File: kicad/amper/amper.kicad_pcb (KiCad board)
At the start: 2 copper layers, 100 x 100 mm, 53 parts, among them J1 Conn_02x05_Odd_Even, J2 Conn_02x05_Odd_Even, J3 Conn_02x05_Odd_Even, J4 USB_C_Receptacle_USB2.0, J5 Conn_01x03, J6 Conn_01x04, J7 Conn_01x05, Q1 FDS9435A, Q2 FDS9435A, SW1 SW_Push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

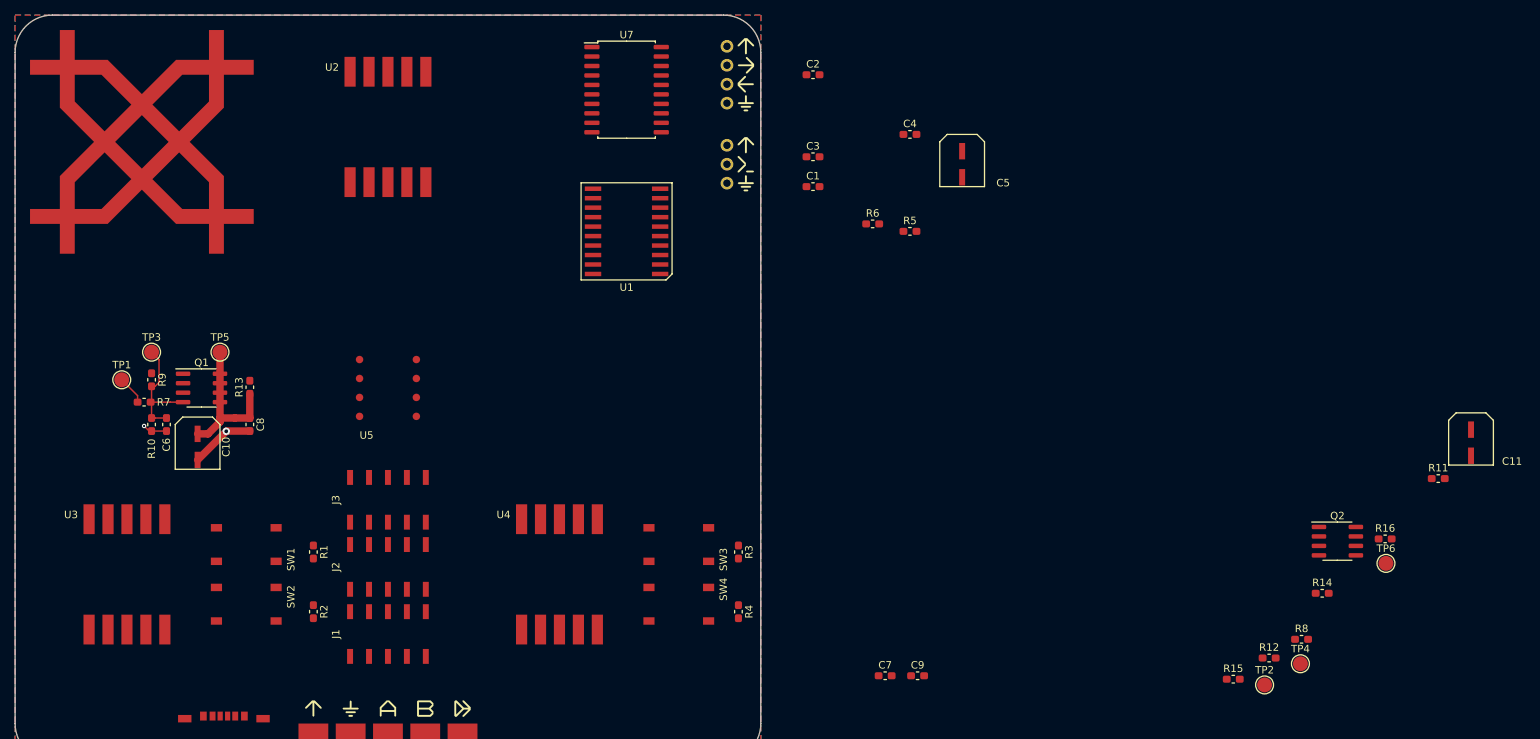
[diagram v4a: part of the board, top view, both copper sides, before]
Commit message: Layed out symetrical 7 seg and driver circuits
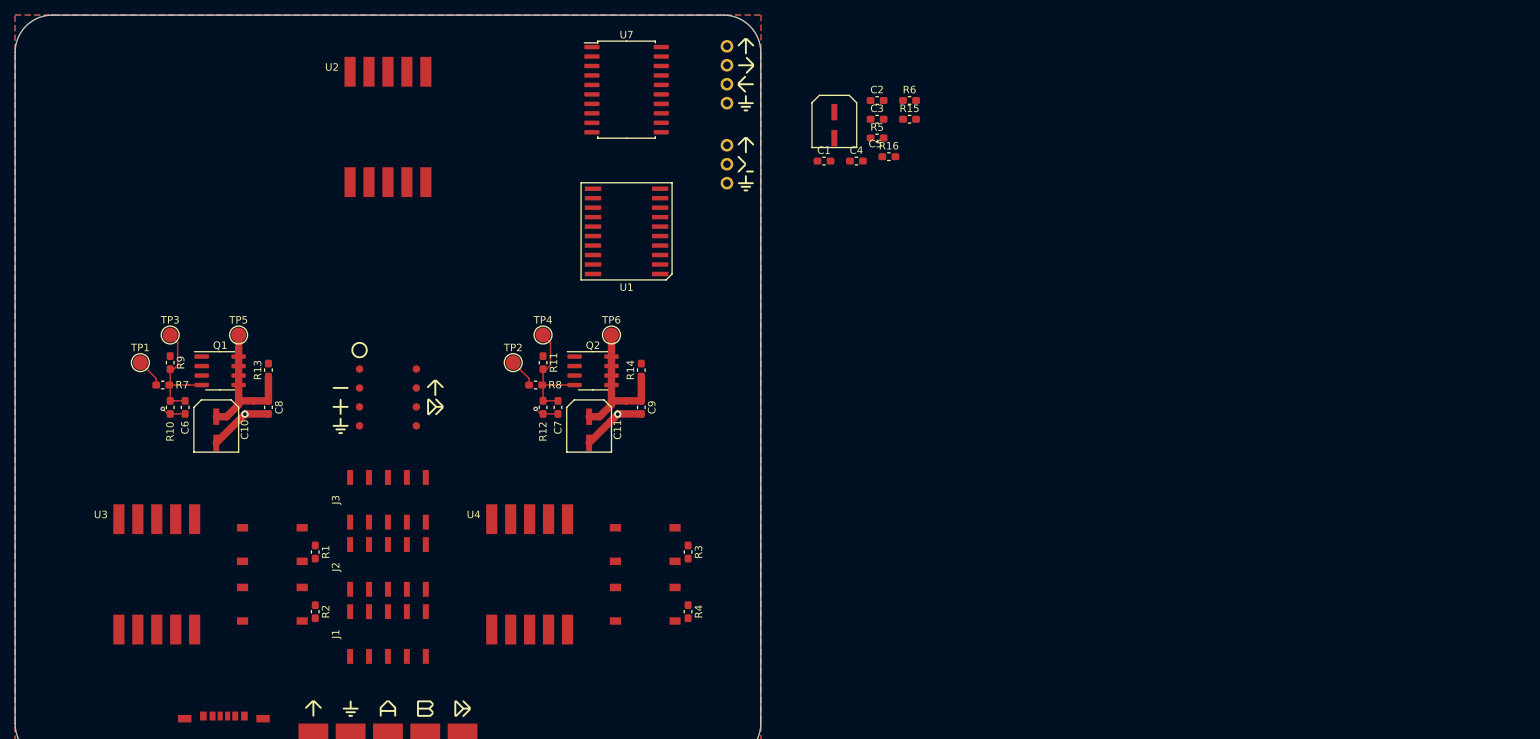
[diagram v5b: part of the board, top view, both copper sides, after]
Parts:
- removed svg2mod: G***, amper:pcb_logo
- U5: footprint amper:114-87-308-41-134161 -> amper:114-87-308-41-134161-generated
- moved R11 121.0 mm to (20.8, -3.40), turned to 270 degrees
- moved C11 118.3 mm to (27.0, 5.61)
- moved TP4 110.7 mm to (20.8, -7.10)
- moved TP2 109.6 mm to (16.8, -3.40)
- moved TP6 108.3 mm to (30.0, -7.10)
- moved R8 108.2 mm to (19.8, -0.40), turned to 180 degrees
- moved R12 103.0 mm to (20.8, 2.60), turned to 270 degrees
- moved Q2 102.4 mm to (27.5, -2.30)
- moved R14 96.1 mm to (34.0, -2.40), turned to 90 degrees
- moved R15 86.7 mm to (69.9, -36.0)
- moved R16 84.0 mm to (67.2, -31.0)
- moved C7 56.7 mm to (22.8, 2.60), turned to 270 degrees
- moved C9 51.7 mm to (34.0, 2.60), turned to 270 degrees
- moved C5 17.9 mm to (59.9, -35.2)
- moved R6 17.3 mm to (69.9, -38.5)
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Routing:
- net /SourceBOut: track 0.00 -> 20.3 mm
- net Net-(C7-Pad1): track 0.00 -> 16.4 mm
- net GND: track 11.9 -> 23.8 mm, vias 2 -> 4
- net /SourceBPwm: track 0.00 -> 3.88 mm

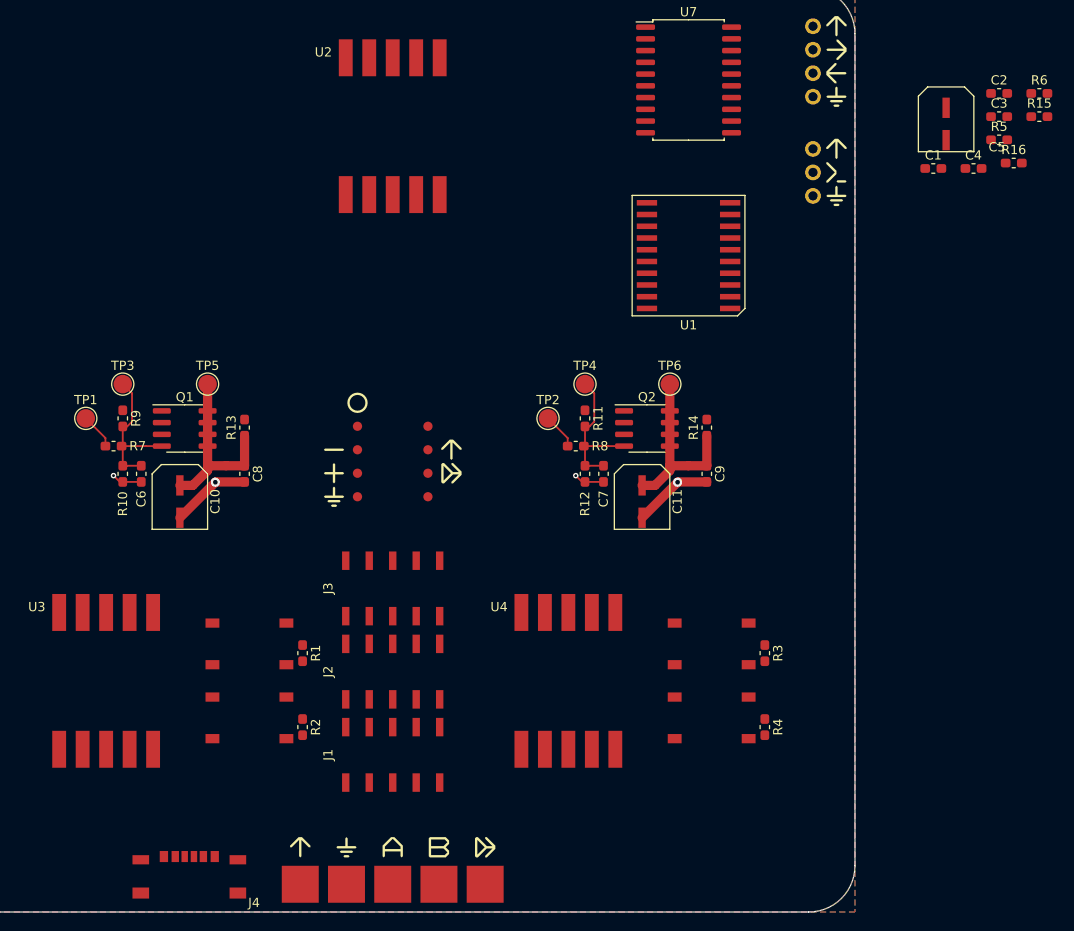
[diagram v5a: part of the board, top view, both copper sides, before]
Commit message: added symbols, Routed very centre of board
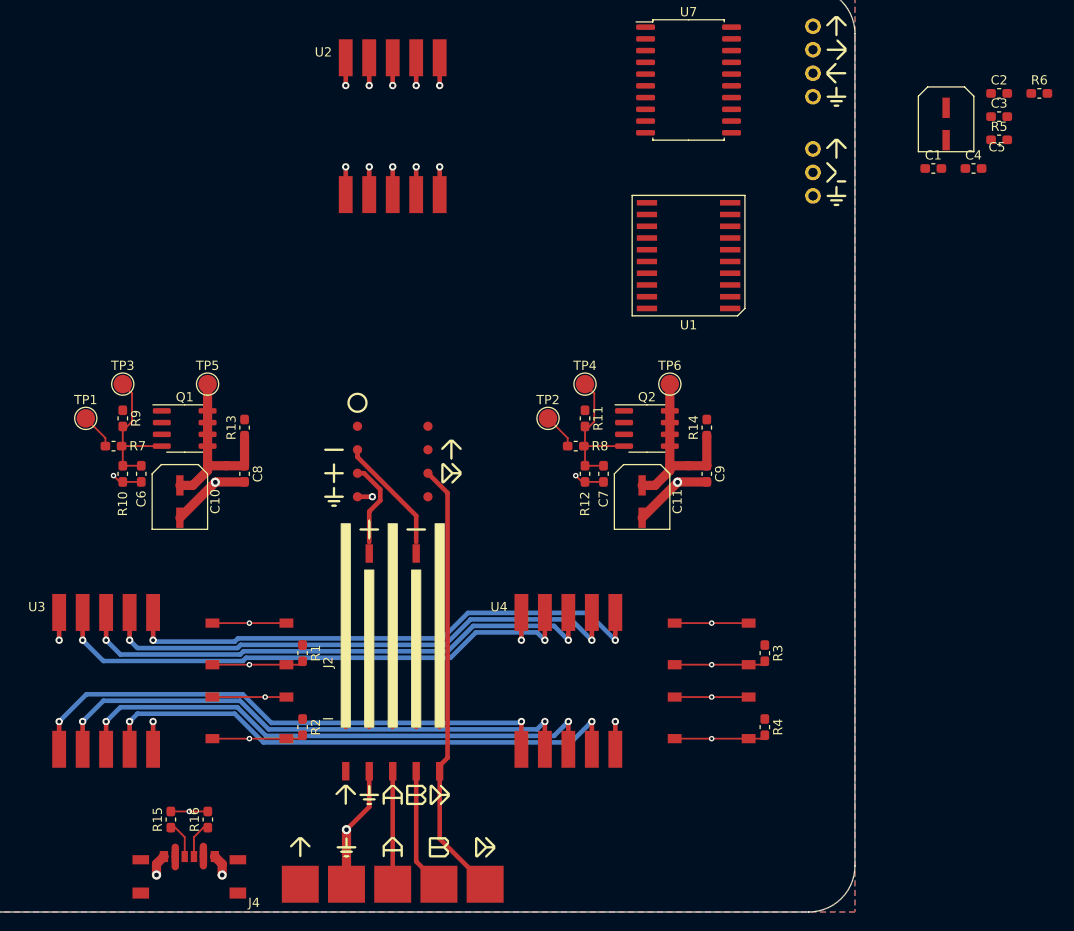
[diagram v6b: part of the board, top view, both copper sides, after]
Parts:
- J1: footprint amper:2.54_2x5_alternate -> amper:2.54_2x5_alternate-source-side
- J3: footprint amper:2.54_2x5_alternate -> amper:2.54_2x5_alternate-opamp-side
- moved R15 120.9 mm to (-24.0, 40.0), turned to 90 degrees
- moved R16 112.4 mm to (-20.0, 40.0), turned to 90 degrees
- moved J3 2.00 mm to (0.00, 13.0)
- moved J2 1.00 mm to (0.00, 23.0)
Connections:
- J1 pad 3: /SourceBOut -> GND
- J1 pad 5: /ResultAdc -> /SourceAOut
- J1 pad 7: /SourceAOut -> /SourceBOut
- J1 pad 9: GND -> /ResultAdc
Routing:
- net /SEG1: track 0.00 -> 61.6 mm, vias 0 -> 3
- net /SEG8: track 0.00 -> 61.6 mm, vias 0 -> 3
- net /SEG5: track 0.00 -> 61.6 mm, vias 0 -> 3
- net /SEG2: track 0.00 -> 61.6 mm, vias 0 -> 3
- net /SEG6: track 0.00 -> 61.6 mm, vias 0 -> 3
- net /SEG4: track 0.00 -> 61.6 mm, vias 0 -> 3
- net /SEG3: track 0.00 -> 61.6 mm, vias 0 -> 3
- net /SEG7: track 0.00 -> 61.6 mm, vias 0 -> 3
- net GND: track 23.8 -> 79.4 mm, vias 4 -> 13
- net /ResultAdc: track 0.00 -> 47.7 mm
- net /R5: track 0.00 -> 20.0 mm
- net /R3: track 0.00 -> 20.0 mm
- net /R1: track 0.00 -> 20.0 mm
- net /R4: track 0.00 -> 14.0 mm
- net /R2: track 0.00 -> 14.0 mm
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
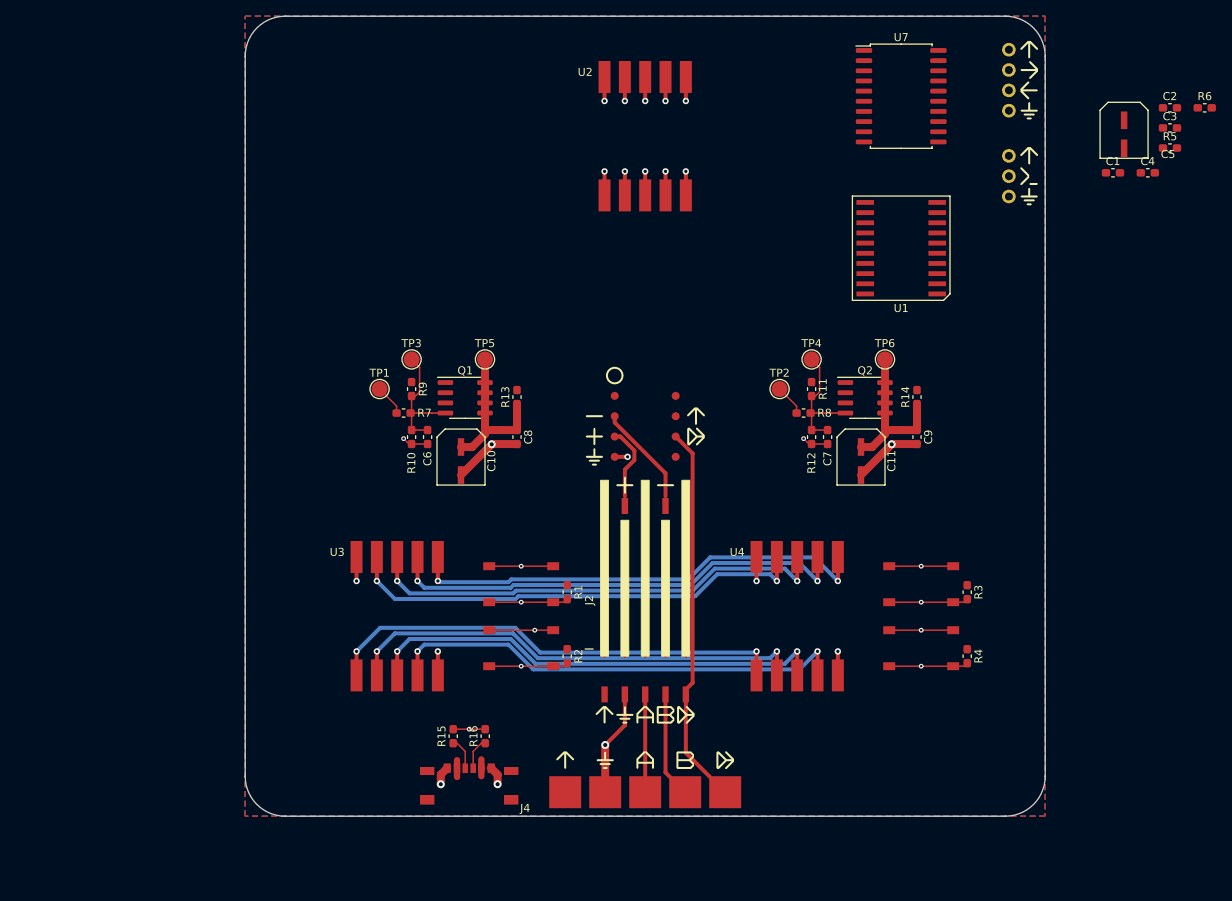
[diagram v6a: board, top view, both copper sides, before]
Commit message: New layout with boxes
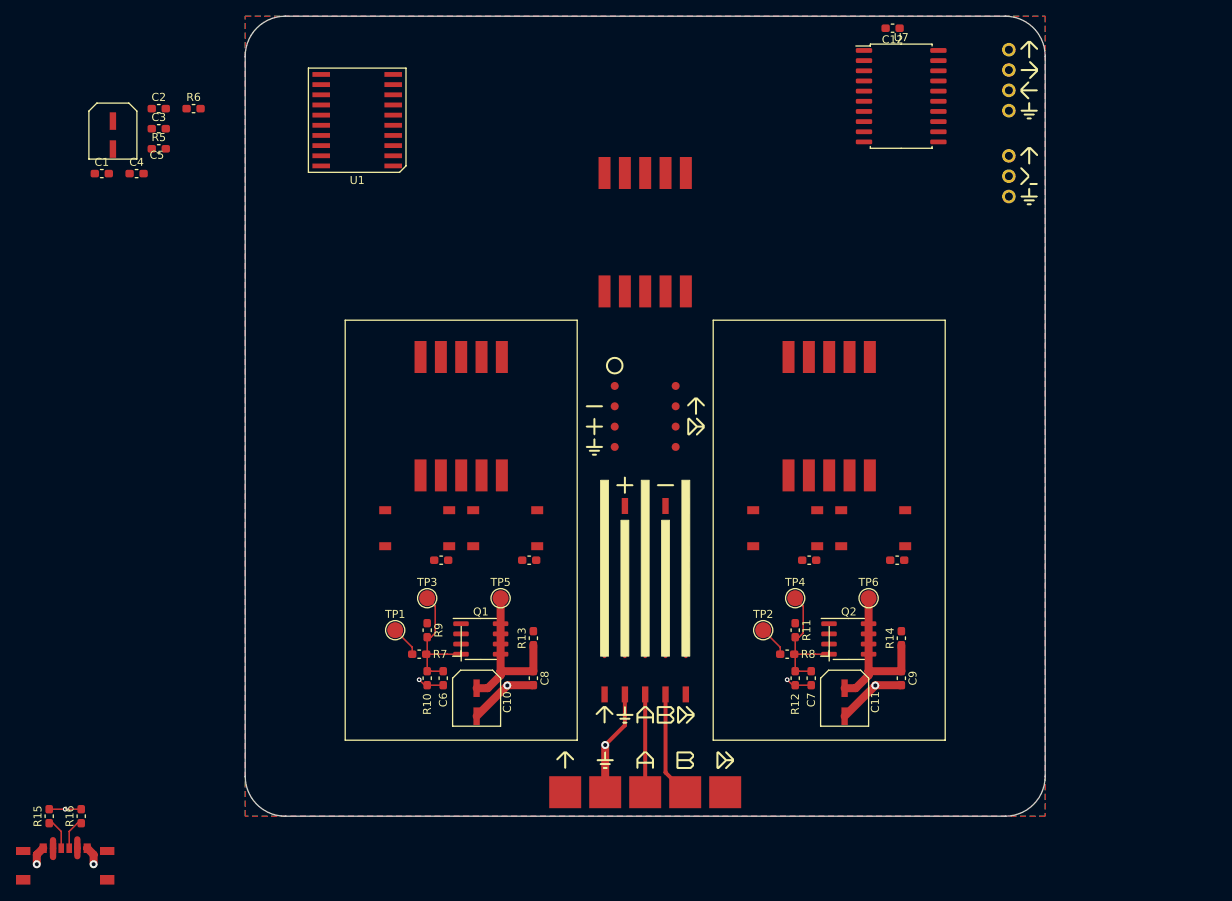
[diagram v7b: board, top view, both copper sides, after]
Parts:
- added C12: 100n, Capacitor_SMD:C_0603_1608Metric_Pad1.05x0.95mm_HandSolder, F.Cu at (30.9, -48.5)
- moved C1 126.4 mm to (-67.9, -30.3)
- moved C2 126.4 mm to (-60.8, -38.4)
- moved C3 126.4 mm to (-60.8, -35.9)
- moved C4 126.4 mm to (-63.6, -30.3)
- moved R5 126.4 mm to (-60.8, -33.4)
- moved R6 126.4 mm to (-56.5, -38.4)
- moved C5 126.4 mm to (-66.5, -35.1)
- moved U1 69.9 mm to (-36.0, -37.0)
- moved J4 51.5 mm to (-72.5, 54.0)
- moved R15 51.5 mm to (-74.5, 50.0)
- moved R16 51.5 mm to (-70.5, 50.0)
- moved C11 30.2 mm to (24.9, 35.8)
- moved C7 30.2 mm to (20.8, 32.8)
- moved Q2 30.2 mm to (25.4, 27.8)
- moved R11 30.2 mm to (18.8, 26.8)
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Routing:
- net /SEG1: track 61.6 -> 0.00 mm, vias 3 -> 0
- net /SEG8: track 61.6 -> 0.00 mm, vias 3 -> 0
- net /SEG5: track 61.6 -> 0.00 mm, vias 3 -> 0
- net /SEG2: track 61.6 -> 0.00 mm, vias 3 -> 0
- net /SEG6: track 61.6 -> 0.00 mm, vias 3 -> 0
- net /SEG4: track 61.6 -> 0.00 mm, vias 3 -> 0
- net /SEG3: track 61.6 -> 0.00 mm, vias 3 -> 0
- net /SEG7: track 61.6 -> 0.00 mm, vias 3 -> 0
- net /ResultAdc: track 47.7 -> 0.00 mm
- net GND: track 79.4 -> 45.8 mm, vias 13 -> 8
- net /V-: track 12.6 -> 0.00 mm
- net Net-(R4-Pad2): track 9.91 -> 0.00 mm, vias 1 -> 0
- net Net-(R3-Pad2): track 9.91 -> 0.00 mm, vias 1 -> 0
- net Net-(R2-Pad2): track 9.91 -> 0.00 mm, vias 1 -> 0
- net Net-(R1-Pad2): track 9.91 -> 0.00 mm, vias 1 -> 0
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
